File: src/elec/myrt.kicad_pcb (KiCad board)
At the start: 2 copper layers, 105.4 x 203.3 mm, 55 parts, among them J1 Spare1, J10 Spare3, J11 Spare4, J2 Spare2, J3 Regular, J4 Regular, J6 USB_B PTH Receptable, J7 Serial 7 Segment Display, J8 Accelerated, J9 Fast, P10 OUT, P11 OUT, P2 POWER_DELIVERY, P3 IN, P4 HMI_Led_Strip, P5 OUT, P6 IN, P7 IN, P8 IN, P9 OUT, SW1 RESET_SW, SW2 START_STOP_SW, U1 ULN2803A, U2 arduino-nano-ATmega328

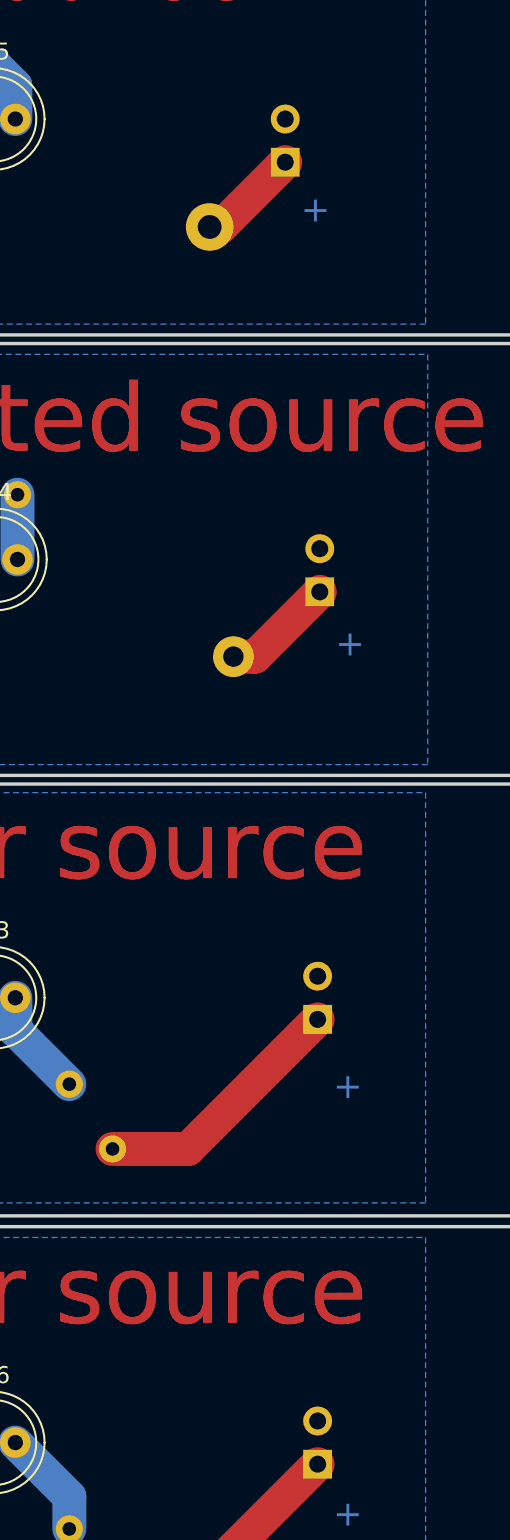
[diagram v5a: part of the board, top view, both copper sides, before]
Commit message: Added via to ease soldering of energy source copper rings connector
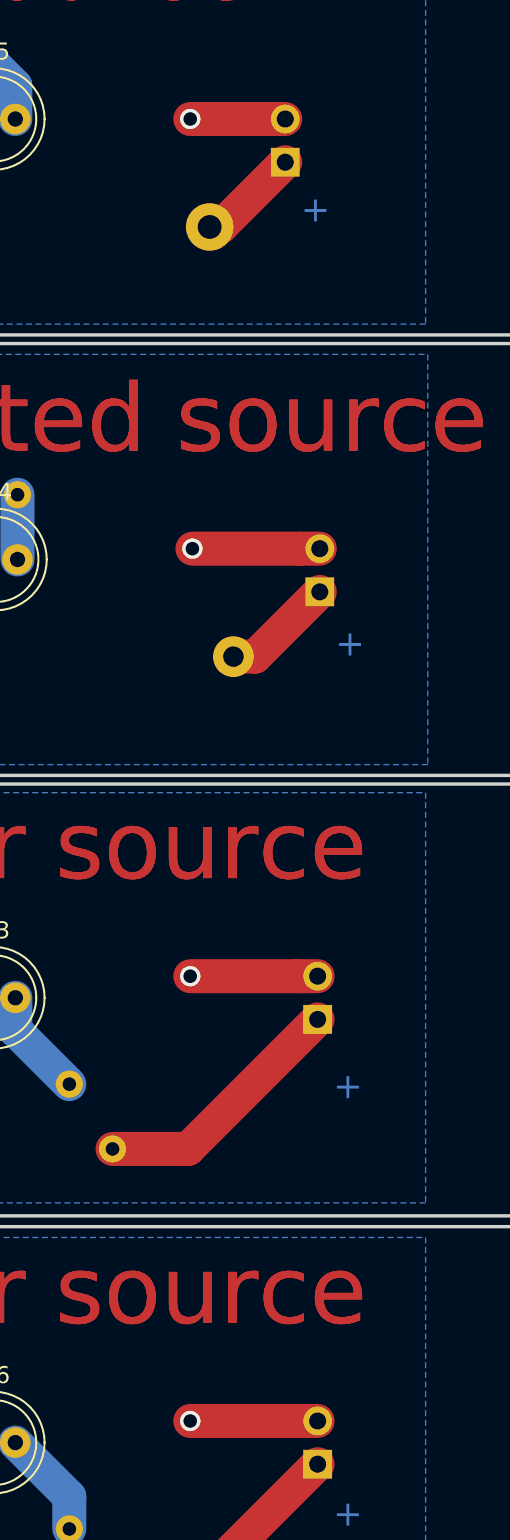
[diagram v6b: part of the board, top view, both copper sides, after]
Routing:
- net /Charging stations/POWER_GND_S2: track 0.00 -> 7.49 mm, vias 0 -> 1
- net /Charging stations/POWER_GND_S4: track 0.00 -> 7.49 mm, vias 0 -> 1
- net /Charging stations/POWER_GND_S1: track 0.00 -> 7.49 mm, vias 0 -> 1
- net /Charging stations/POWER_GND_S3: track 0.00 -> 5.59 mm, vias 0 -> 1
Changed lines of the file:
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@@
     (thickness 1.6)
     (drawings 99)
-    (tracks 283)
+    (tracks 295)
     (zones 0)
     (modules 55)
@@
     (pad_drill 0.762)
     (pad_to_mask_clearance 0.2)
-    (aux_axis_origin 0 0)
+    (aux_axis_origin 54.991 244.348)
+    (grid_origin 54.991 244.348)
     (visible_elements FFFFF7FF)
     (pcbplotparams
       (layerselection 0x01000_ffffffff)
       (usegerberextensions false)
-      (usegerberattributes false)
-      (usegerberadvancedattributes false)
+      (usegerberattributes true)
+      (usegerberadvancedattributes true)
       (creategerberjobfile true)
       (excludeedgelayer true)
@@
       (viasonmask false)
       (mode 1)
-      (useauxorigin false)
+      (useauxorigin true)
       (hpglpennumber 1)
       (hpglpenspeed 20)
@@
   (segment (start 82.55 113.411) (end 87.63 113.411) (width 2) (layer B.Cu) (net 12) (status 30))
   (segment (start 82.55 118.491) (end 87.63 118.491) (width 2) (layer B.Cu) (net 13) (status 30))
+  (segment (start 121.666 204.216) (end 120.463919 204.216) (width 2) (layer F.Cu) (net 14))
+  (segment (start 120.463919 204.216) (end 114.173 204.216) (width 2) (layer F.Cu) (net 14))
+  (via (at 114.173 204.216) (size 1.2) (drill 0.8) (layers F.Cu B.Cu) (net 14))
+  (segment (start 121.793 179.07) (end 120.590919 179.07) (width 2) (layer F.Cu) (net 15))
+  (segment (start 120.590919 179.07) (end 114.3 179.07) (width 2) (layer F.Cu) (net 15))
+  (via (at 114.3 179.07) (size 1.2) (drill 0.8) (layers F.Cu B.Cu) (net 15))
+  (segment (start 119.761 153.797) (end 118.558919 153.797) (width 2) (layer F.Cu) (net 16))
+  (segment (start 118.558919 153.797) (end 114.173 153.797) (width 2) (layer F.Cu) (net 16))
+  (via (at 114.173 153.797) (size 1.2) (drill 0.8) (layers F.Cu B.Cu) (net 16))
   (segment (start 94.361 214.376) (end 94.361 210.566) (width 2) (layer B.Cu) (net 17) (status 10))
   (segment (start 95.631 209.296) (end 96.901 210.566) (width 2) (layer B.Cu) (net 17) (status 20))
@@
   (segment (start 81.41863 121.031) (end 76.454 116.06637) (width 1) (layer B.Cu) (net 25))
   (segment (start 76.454 116.06637) (end 76.454 92.929558) (width 1) (layer B.Cu) (net 25))
+  (segment (start 121.666 230.378) (end 120.463919 230.378) (width 2) (layer F.Cu) (net 26))
+  (segment (start 120.463919 230.378) (end 114.173 230.378) (width 2) (layer F.Cu) (net 26))
+  (via (at 114.173 230.378) (size 1.2) (drill 0.8) (layers F.Cu B.Cu) (net 26))
   (segment (start 107.061 234.823) (end 103.886 231.648) (width 2) (layer B.Cu) (net 27) (status 20))
   (segment (start 107.061 236.728) (end 107.061 234.823) (width 2) (layer B.Cu) (net 27) (status 10))
